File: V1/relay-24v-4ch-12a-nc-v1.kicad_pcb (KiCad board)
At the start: 2 copper layers, 53 x 67.8 mm, 23 parts, among them J1 DG141V-2.54-6P, J2 DB142V-5.08-4P, J3 DB142V-5.08-4P, K1 Songle_SRD_1B, K2 Songle_SRD_1B, K3 Songle_SRD_1B, K4 Songle_SRD_1B

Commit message: Creating layout
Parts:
- added J2: DB141V-2.54-4P, Tales:TerminalBlock_Dibo_DB141V-2.54-4P_1x04_P2.54mm_Vertical, F.Cu at (189.5, 67.9)
- J1: value DG141V-2.54-6P -> DB141V-2.54-2P; footprint Tales:TerminalBlock_Dibo_DB141V-2.54-6P_1x06_P2.54mm_Vertical -> Tales:TerminalBlock_Dibo_DB141V-2.54-2P_1x02_P2.54mm_Vertical
- moved D8 31.8 mm to (178.7, 78.0)
- moved K4 23.9 mm to (183.0, 82.5), turned to -90 degrees
- moved RV1 22.2 mm to (135.0, 103.5), turned to 0 degrees
- moved D6 21.4 mm to (162.7, 78.0)
- moved K2 20.6 mm to (151.0, 82.5), turned to -90 degrees
- moved RV3 18.8 mm to (167.0, 103.5), turned to 0 degrees
- moved J4 14.0 mm to (170.0, 122.0)
- moved D4 11.2 mm to (146.7, 78.0)
- moved RV4 9.64 mm to (183.0, 103.5), turned to 0 degrees
- moved K1 9.61 mm to (135.0, 82.5), turned to -90 degrees
- moved J3 9.06 mm to (138.0, 122.0)
- moved K3 3.93 mm to (167.0, 82.5), turned to -90 degrees
- moved R1 3.73 mm to (151.2, 70.5)
- moved R2 3.73 mm to (151.2, 72.0)
- moved R3 3.73 mm to (151.2, 73.5)
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- renumbered J2 to J3, J3 to J4
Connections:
- J1 pad 1: Net-(D7-K) -> +24V
- J1 pad 2: Net-(D5-K) -> +24V
- J3 pad 2: Net-(J2-Pin_2) -> Net-(J3-Pin_2)
- J3 pad 4: Net-(J2-Pin_4) -> Net-(J3-Pin_4)
- J4 pad 2: Net-(J3-Pin_2) -> Net-(J4-Pin_2)
- J4 pad 4: Net-(J3-Pin_4) -> Net-(J4-Pin_4)
- RV1 pad 2: Net-(J2-Pin_2) -> Net-(J3-Pin_2)
- RV2 pad 2: Net-(J2-Pin_4) -> Net-(J3-Pin_4)
- RV3 pad 2: Net-(J3-Pin_2) -> Net-(J4-Pin_2)
- RV4 pad 2: Net-(J3-Pin_4) -> Net-(J4-Pin_4)
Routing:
- net Net-(J4-Pin_1): track 0.00 -> 81.5 mm
- net Net-(J3-Pin_1): track 0.00 -> 81.5 mm
- net Net-(J4-Pin_3): track 0.00 -> 81.4 mm
- net Net-(J3-Pin_3): track 0.00 -> 81.4 mm
- net Net-(J4-Pin_2): track 0.00 -> 53.8 mm
- net Net-(J3-Pin_2): track 0.00 -> 53.8 mm
- net Net-(J4-Pin_4): track 0.00 -> 53.7 mm
- net Net-(J3-Pin_4): track 0.00 -> 53.7 mm
- net +24V: track 24.3 -> 31.0 mm
- net Net-(D7-K): track 5.08 -> 0.00 mm
- net Net-(D5-K): track 5.08 -> 0.00 mm
- net Net-(D3-K): track 5.08 -> 0.00 mm
- net Net-(D1-K): track 5.08 -> 0.00 mm
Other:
- board size 53 x 67.8 mm -> 68 x 67.8 mm
- board text added: "ATTENTION!! NC CONTACTS"
- board text added: "SUPORTES PCI METALTEX SP7 1x pé macho 9 mm 1x pé fêmea 9 mm 1x espaçador 30 mm 1x espaçador 20 mm Comprimento total 68 mm Largura da placa 67,8 mm"
- board text removed: "SUPORTES PCI METALTEX SP7 1x pé macho 9 mm 1x pé fêmea 9 mm 1x espaçador 30 mm 1x espaçador 5 mm Comprimento total 53 mm Largura da placa 67,8 mm"

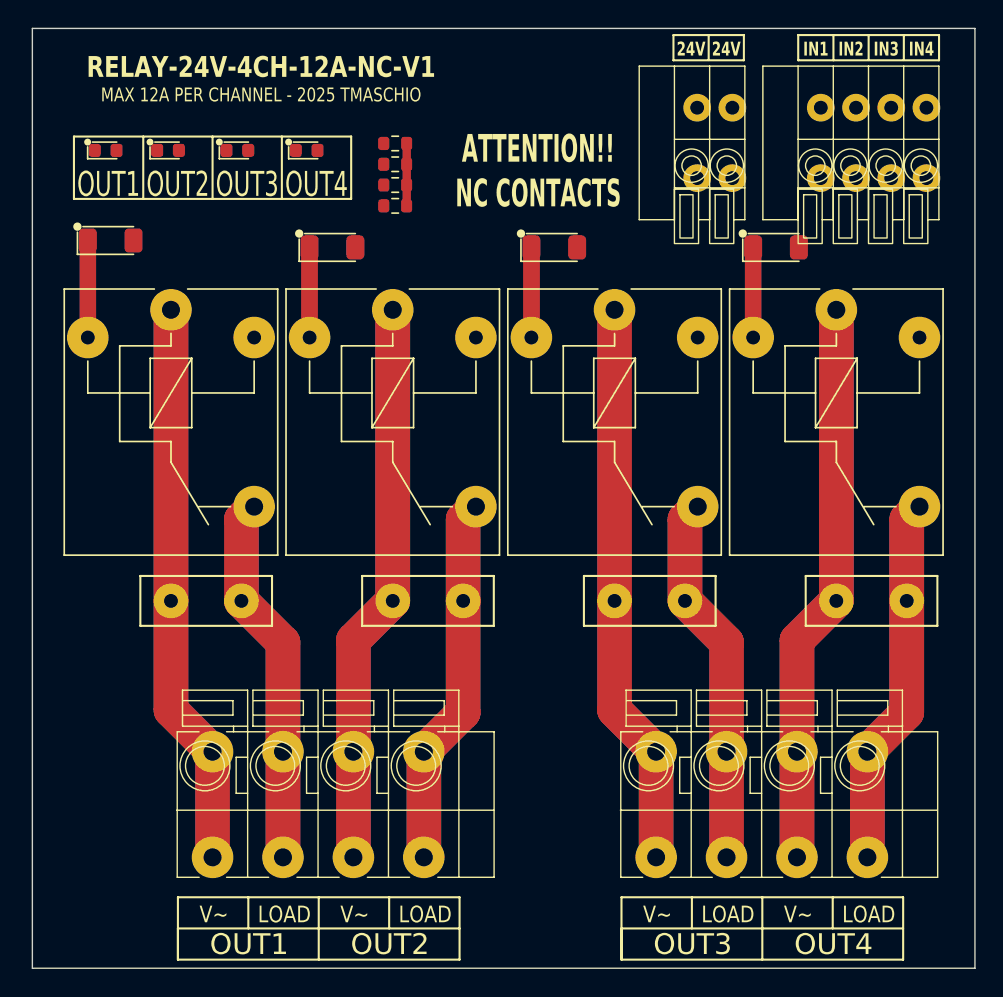
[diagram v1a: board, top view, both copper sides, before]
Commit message: Updated connectors
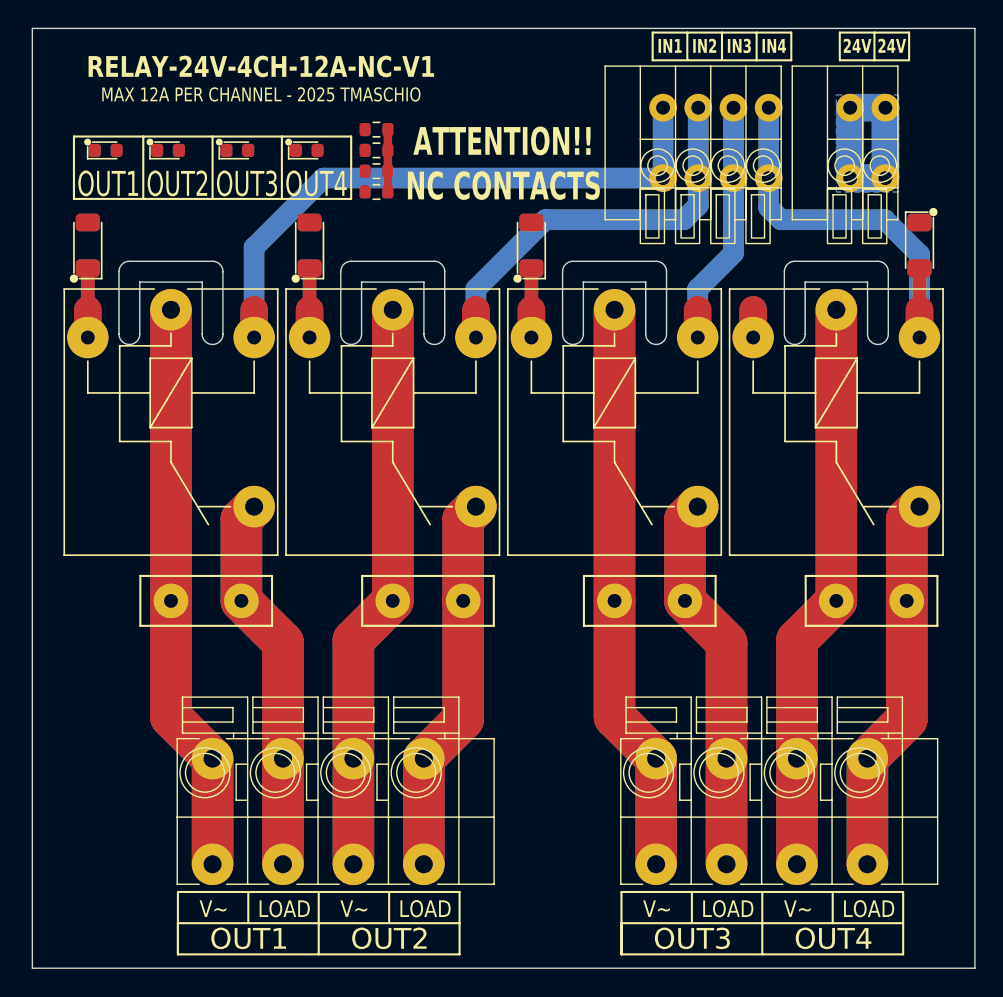
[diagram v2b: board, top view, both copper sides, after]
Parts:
- R1, R2, R3, R4: value 5k6/100mW -> 6k8/100mW
- moved J2 11.4 mm to (178.1, 67.9)
- moved J1 11.0 mm to (186.5, 67.9)
- moved D8 10.4 mm to (189.0, 77.8), turned to -90 degrees
- moved D2 1.69 mm to (129.0, 77.8), turned to 90 degrees
- moved R1 1.68 mm to (149.8, 69.5)
- moved R2 1.68 mm to (149.8, 71.0)
- moved R3 1.68 mm to (149.8, 72.5)
- moved R4 1.68 mm to (149.8, 74.0)
- moved D4 1.66 mm to (145.0, 77.8), turned to 90 degrees
- moved D6 1.66 mm to (161.0, 77.8), turned to 90 degrees
- moved J3 0.50 mm to (138.0, 122.5)
- moved J4 0.50 mm to (170.0, 122.5)
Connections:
- J2 pad 1: Net-(D1-K) -> Net-(D7-K)
- J2 pad 2: Net-(D3-K) -> Net-(D5-K)
- J2 pad 3: Net-(D5-K) -> Net-(D3-K)
- J2 pad 4: Net-(D7-K) -> Net-(D1-K)
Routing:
- net Net-(D1-K): track 0.00 -> 45.2 mm
- net Net-(D3-K): track 0.00 -> 31.1 mm
- net Net-(D7-K): track 0.00 -> 30.6 mm
- net Net-(D5-K): track 0.00 -> 19.6 mm
- net +24V: track 31.0 -> 36.7 mm
- net Net-(J4-Pin_4): track 53.7 -> 54.7 mm
- net Net-(J4-Pin_3): track 81.4 -> 82.4 mm
- net Net-(J4-Pin_2): track 53.8 -> 54.8 mm
- net Net-(J4-Pin_1): track 81.5 -> 82.5 mm
- net Net-(J3-Pin_4): track 53.7 -> 54.7 mm
- net Net-(J3-Pin_3): track 81.4 -> 82.4 mm
- net Net-(J3-Pin_2): track 53.8 -> 54.8 mm
- net Net-(J3-Pin_1): track 81.5 -> 82.5 mm
- added copper zone on B.Cu, net +24V
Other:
- outline, holes or cut-outs redrawn

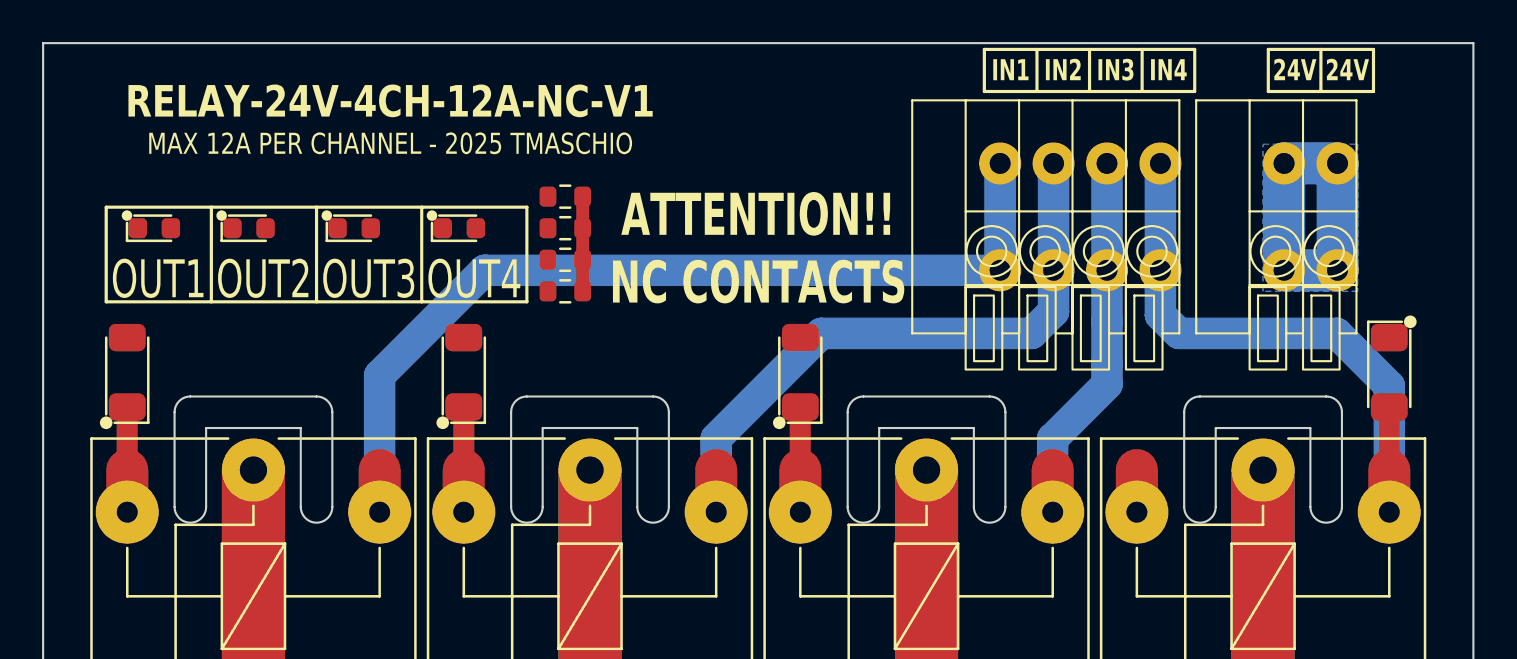
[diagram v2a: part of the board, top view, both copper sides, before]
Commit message: Update relay-24v-4ch-12a-nc-v1.kicad_pcb
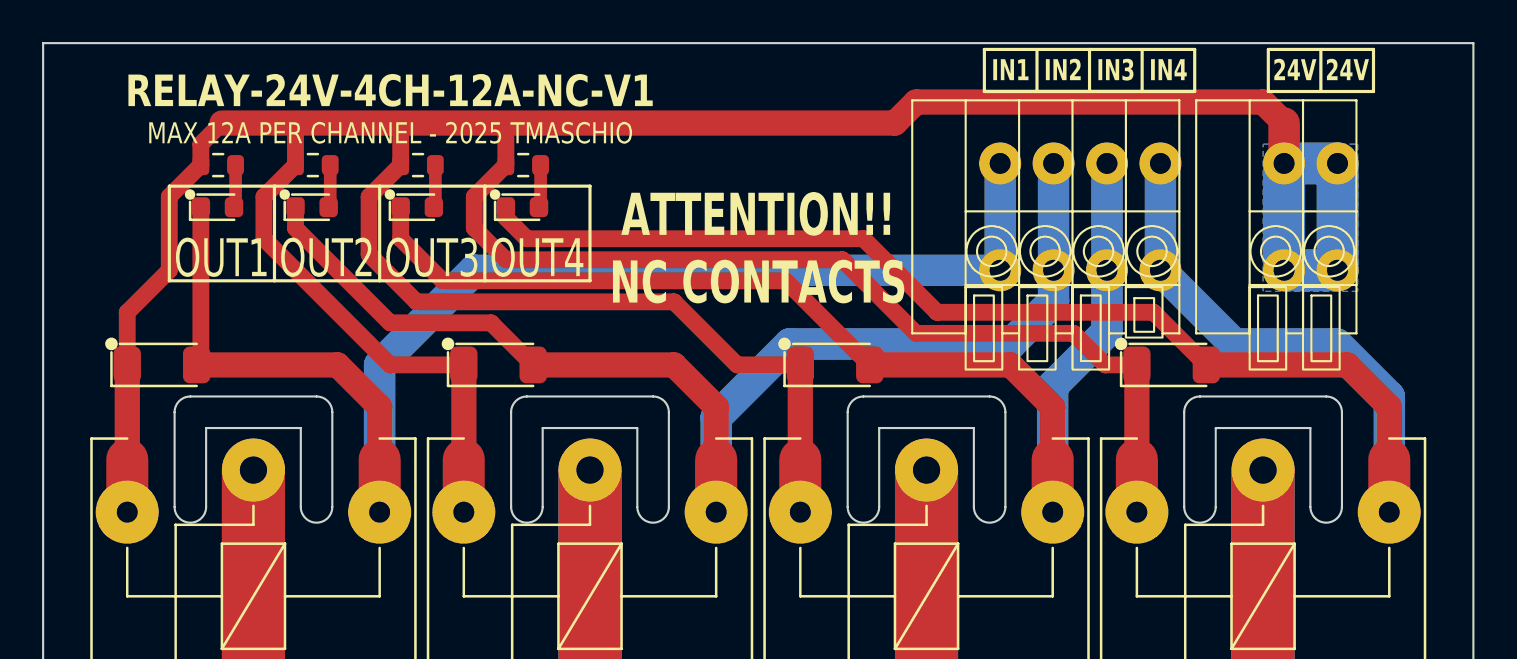
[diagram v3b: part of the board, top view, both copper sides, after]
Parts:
- moved R1 16.6 mm to (133.3, 68.0), turned to 0 degrees
- moved R2 12.4 mm to (137.8, 68.0), turned to 0 degrees
- moved D8 10.4 mm to (178.7, 77.5), turned to 0 degrees
- moved R3 8.32 mm to (142.8, 68.0), turned to 0 degrees
- moved R4 6.32 mm to (147.8, 68.0), turned to 0 degrees
- moved D1 3.16 mm to (133.3, 70.0)
- moved D3 3.16 mm to (137.8, 70.0)
- moved D5 3.16 mm to (142.8, 70.0)
- moved D7 3.16 mm to (147.8, 70.0)
- moved D2 1.69 mm to (130.7, 77.5), turned to 0 degrees
- moved D4 1.69 mm to (146.7, 77.5), turned to 0 degrees
- moved D6 1.69 mm to (162.7, 77.5), turned to 0 degrees
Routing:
- net +24V: track 36.7 -> 197.3 mm
- net Net-(D7-K): track 30.6 -> 75.3 mm
- net Net-(D5-K): track 19.6 -> 58.5 mm
- net Net-(D3-K): track 31.1 -> 58.9 mm
- net Net-(D1-K): track 45.2 -> 65.6 mm
- net Net-(D7-A): track 0.00 -> 2.03 mm
- net Net-(D5-A): track 0.00 -> 2.03 mm
- net Net-(D3-A): track 0.00 -> 2.03 mm
- net Net-(D1-A): track 0.00 -> 2.03 mm
